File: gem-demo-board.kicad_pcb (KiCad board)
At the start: 6 copper layers, 56 x 66 mm, 151 parts, among them J1 3220-10-0100-00, J10 0473460001, J2 DF13A-2P-1.25H, J3 3220-10-0100-00, J4 2x20_Header_Female, J5 0473460001, J6 556500488, J7 556500488, J8 WE_686115148922, J9 WE_686115148922_FLIPPED, U1 MCP1700T-3302E_TT, U2 NTS0104BQ, U3 NTS0104BQ, U4 NTS0104BQ, U5 93LC56CT-IMC, U6 FT4232HQ, U7 NTB0104BQ, U8 NTB0104BQ, Y1 ASFLMB-12.000MHZ-LC-T

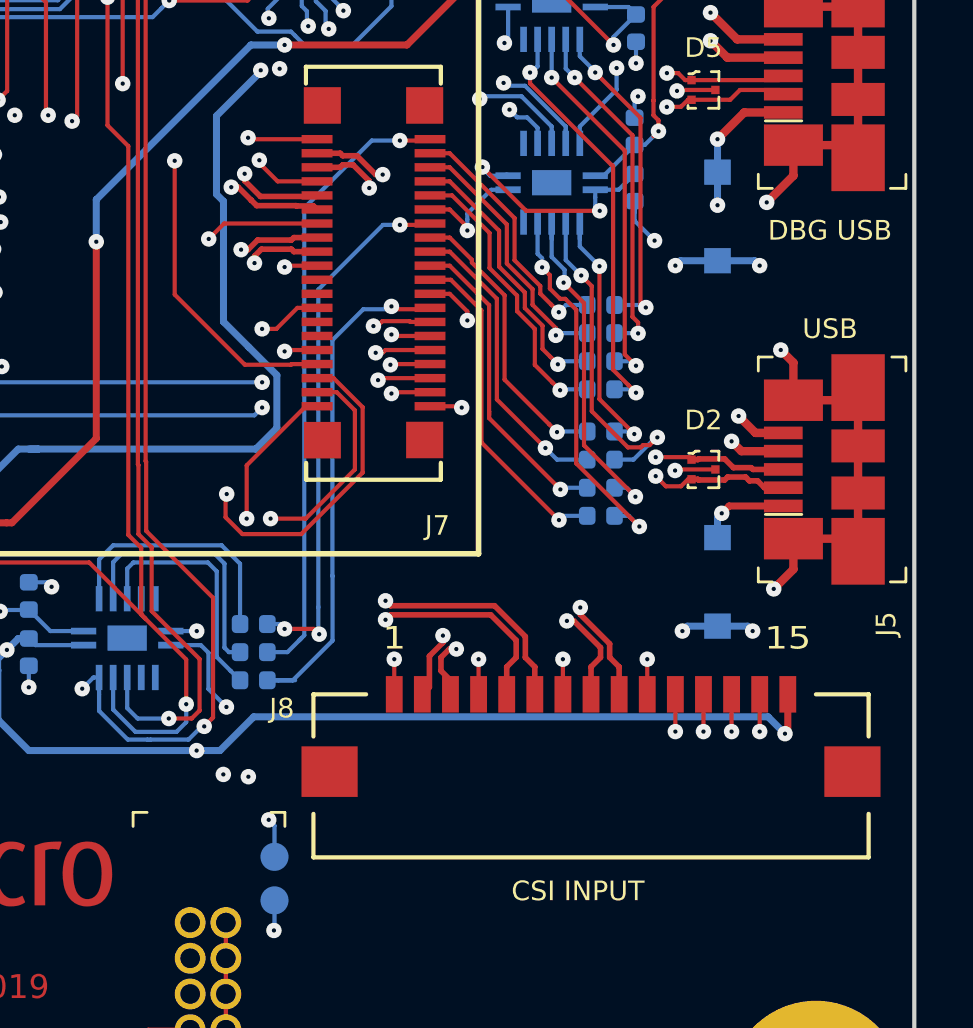
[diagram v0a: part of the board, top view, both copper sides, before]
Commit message: Flipped CSI input connector
Use camera FFC with pads on the same side now
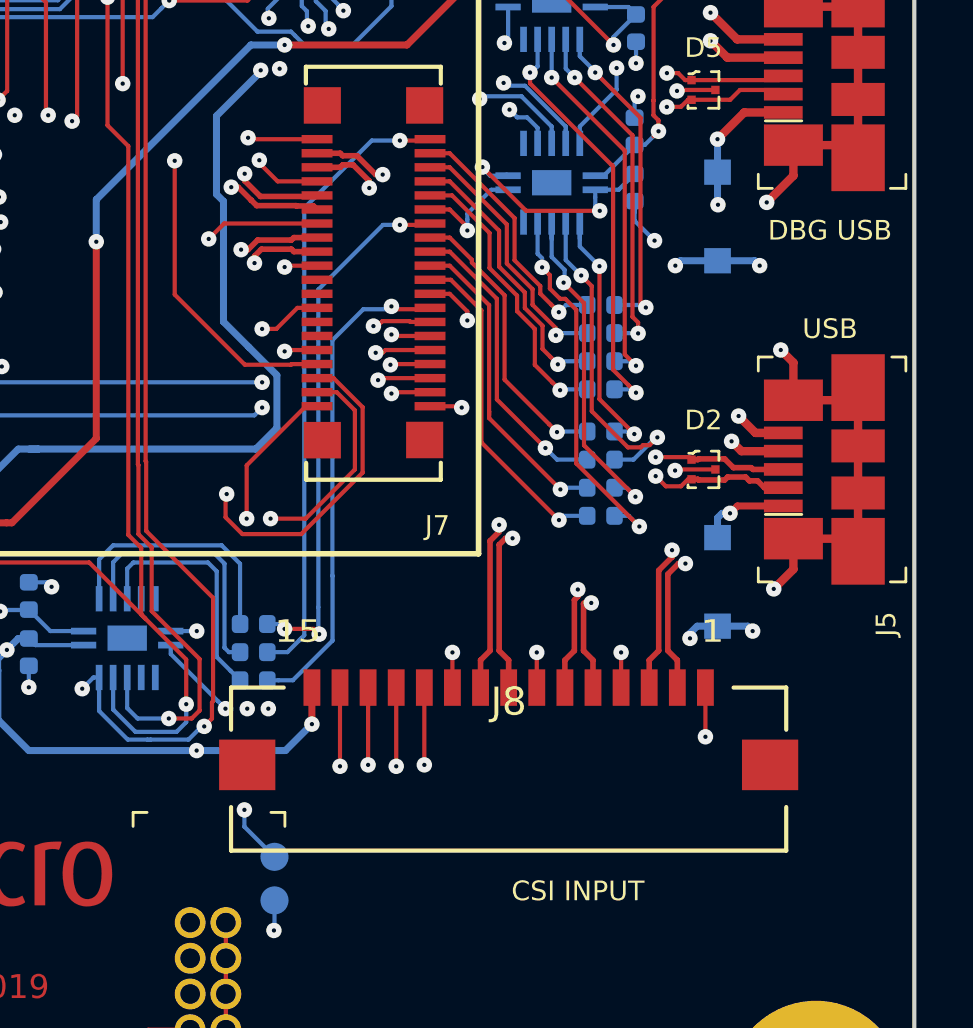
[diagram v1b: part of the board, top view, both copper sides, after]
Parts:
- J8: value WE_686115148922 -> WE_686115148922_FLIPPED; footprint zglue-demo-board-footprints:WE_686115148922 -> zglue-demo-board-footprints:WE_686115148922_FLIPPED
- moved J8 2.94 mm to (69.4, 78.0)
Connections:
- C18 pad 2: GND -> Net-(C18-Pad2)
- C19 pad 2: GND -> Net-(C19-Pad2)
- C21 pad 1: /VPHY -> Net-(C21-Pad1)
- C22 pad 1: /VPLL -> Net-(C22-Pad1)
- C25 pad 1: /VPHY -> Net-(C25-Pad1)
- C26 pad 1: /VPLL -> Net-(C26-Pad1)
- R4 pad 2: /3V3_FTDI -> Net-(R4-Pad2)
- R6 pad 2: /3V3_FTDI -> Net-(R6-Pad2)
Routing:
- net /CAM_SDA_IN: track 56.7 -> 90.8 mm
- net /3V3_SYS: track 250.6 -> 233.3 mm
- net /CAM_SCL_IN: track 56.9 -> 73.6 mm
- net /CSI_D1_IN_P: track 36.6 -> 44.7 mm
- net /CSI_D1_IN_N: track 36.6 -> 44.7 mm
- net /CAM_CLK_IN: track 20.7 -> 14.1 mm
- net /CAM_GPIO_IN: track 18.5 -> 12.7 mm
- net /CSI_D2_IN_N: track 36.6 -> 40.3 mm
- net /VCCIO3: track 84.3 -> 80.9 mm
- net /CSI_D2_IN_P: track 36.6 -> 39.8 mm
- net /CSI_CLK_IN_P: track 37.0 -> 35.3 mm
- net /CSI_CLK_IN_N: track 36.6 -> 35.3 mm
- net /DONE: track 54.9 -> 53.9 mm
- net /VCCIO2: track 66.1 -> 65.3 mm
- net GND: track 180.6 -> 179.8 mm, vias 79 -> 77
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
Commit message: Minor changes
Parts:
- moved R54 3.60 mm to (66.8, 39.5)
- moved R56 1.20 mm to (66.8, 42.0)
- moved R57 1.20 mm to (66.8, 40.8)
- moved R55 1.20 mm to (66.8, 43.1)
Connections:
- D10 pad 1: /3V3_SYS -> Net-(D10-Pad1)
- D11 pad 1: /3V3_SYS -> Net-(D11-Pad1)
- D8 pad 1: /3V3_SYS -> Net-(D8-Pad1)
- D9 pad 1: /3V3_SYS -> Net-(D9-Pad1)
- J8 pad 11: /CAM_GPIO_IN -> /3V3_SYS
- R48 pad 1: /DBG_TX -> /DBG_RX
- R49 pad 1: /DBG_RX -> /DBG_TX
- TP20 pad 1: /CAM_GPIO_IN -> /3V3_SYS
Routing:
- net /3V3_SYS: track 233.3 -> 254.3 mm, vias 19 -> 21
- net /CAM_GPIO_IN: track 12.7 -> 0.00 mm, vias 2 -> 0
- net /CSI_CLK_IN_N: track 35.3 -> 42.3 mm
- net /CSI_CLK_IN_P: track 35.3 -> 42.3 mm
- net /CAM_SDA_OUT: track 20.7 -> 17.6 mm, vias 3 -> 2
- net /CSI_D1_IN_P: track 44.7 -> 42.3 mm
- net /CSI_D1_IN_N: track 44.7 -> 42.3 mm
- net /CSI_D2_IN_P: track 39.8 -> 41.8 mm
- net /CSI_D2_IN_N: track 40.3 -> 41.8 mm
- net /I2C_1_SCL_3V3: track 20.4 -> 19.4 mm
- net /CAM_SCL_OUT: track 17.5 -> 18.5 mm
- net /DBG_TX: track 4.89 -> 5.64 mm
- net /I2C_1_SDA_3V3: track 21.6 -> 22.1 mm
- net /CAM_SDA_IN: track 90.8 -> 90.3 mm
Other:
- net class Default: clearance 0.125 -> 0.12
- rule trace_clearance: 0.125 -> 0.12

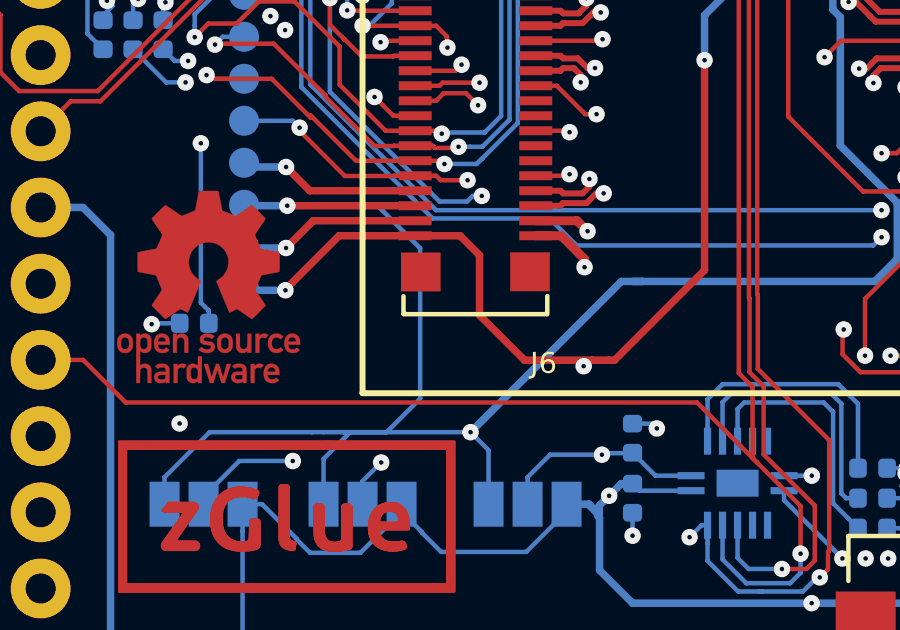
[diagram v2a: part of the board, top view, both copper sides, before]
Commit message: Disconnected 3v3_sys from GEM system chip with R60
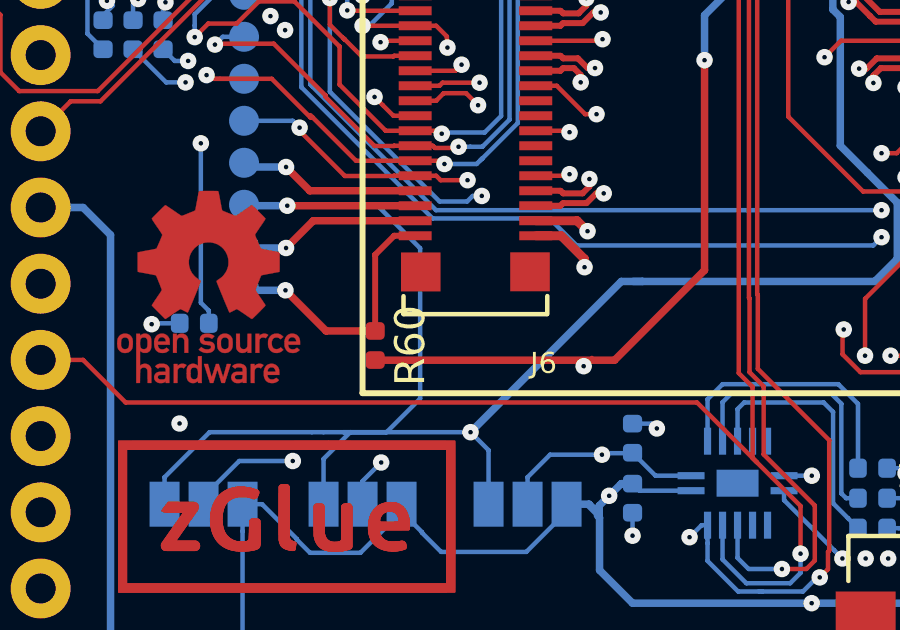
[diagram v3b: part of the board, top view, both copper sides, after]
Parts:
- added R60: R_0R_0402, zglue-demo-board-footprints:0402-res, F.Cu at (43.7, 71.7)
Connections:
- J6 pad 40: /3V3_SYS -> Net-(J6-Pad40)
- TP4 pad 1: /3V3_SYS -> Net-(J6-Pad40)
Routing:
- net Net-(J6-Pad40): track 0.00 -> 9.09 mm, vias 0 -> 1
- net /3V3_SYS: track 254.3 -> 246.2 mm, vias 21 -> 20
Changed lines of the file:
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@@
     (thickness 1.6)
     (drawings 30)
-    (tracks 4089)
+    (tracks 4087)
     (zones 0)
-    (modules 151)
-    (nets 225)
+    (modules 152)
+    (nets 226)
   )
   (page A4)
@@
   (net 223 "Net-(D10-Pad1)")
   (net 224 "Net-(D11-Pad1)")
+  (net 225 "Net-(J6-Pad40)")
   (net_class Default "This is the default net class."
     (clearance 0.12)
@@
     (add_net "Net-(J4-Pad7)")
     (add_net "Net-(J4-Pad8)")
+    (add_net "Net-(J6-Pad40)")
     (add_net "Net-(R10-Pad2)")
     (add_net "Net-(R11-Pad1)")
@@
     (add_net "Net-(U8-Pad9)")
   )
+  (module zglue-demo-board-footprints:0402-res (layer F.Cu)
+    (at 43.72 71.66 270)
+    (descr "Resistor SMD 0402 (1005 Metric), square (rectangular) end terminal, IPC_7351 nominal, (Body size source: http://www.tortai-tech.com/upload/download/2011102023233369053.pdf), generated with kicad-footprint-generator")
+    (tags resistor)
+    (attr smd)
+    (fp_text reference R60 (at 0 -1.17 90) (layer F.SilkS)
+      (effects (font (size 1 1) (thickness 0.15)))
+    )
+    (fp_text value R_0R_0402 (at 0 1.17 90) (layer F.Fab)
+      (effects (font (size 1 1) (thickness 0.15)))
+    )
+    (fp_text user %R (at 0 0 90) (layer F.Fab)
+      (effects (font (size 0.25 0.25) (thickness 0.04)))
+    )
+    (fp_line (start 0.93 0.47) (end -0.93 0.47) (layer F.CrtYd) (width 0.05))
+    (fp_line (start 0.93 -0.47) (end 0.93 0.47) (layer F.CrtYd) (width 0.05))
+    (fp_line (start -0.93 -0.47) (end 0.93 -0.47) (layer F.CrtYd) (width 0.05))
+    (fp_line (start -0.93 0.47) (end -0.93 -0.47) (layer F.CrtYd) (width 0.05))
+    (fp_line (start 0.5 0.25) (end -0.5 0.25) (layer F.Fab) (width 0.1))
+    (fp_line (start 0.5 -0.25) (end 0.5 0.25) (layer F.Fab) (width 0.1))
+    (fp_line (start -0.5 -0.25) (end 0.5 -0.25) (layer F.Fab) (width 0.1))
+    (fp_line (start -0.5 0.25) (end -0.5 -0.25) (layer F.Fab) (width 0.1))
+    (pad 2 smd roundrect (at 0.485 0 270) (size 0.59 0.64) (layers F.Cu F.Paste F.Mask) (roundrect_rratio 0.25)
+      (net 8 /3V3_SYS))
+    (pad 1 smd roundrect (at -0.485 0 270) (size 0.59 0.64) (layers F.Cu F.Paste F.Mask) (roundrect_rratio 0.25)
+      (net 225 "Net-(J6-Pad40)"))
+    (model ${KIPRJMOD}/lib/3d-models/0402-res.step
+      (offset (xyz 0 0 -0.01))
+      (scale (xyz 1 1 1))
+      (rotate (xyz 0 0 0))
+    )
+  )
   (module zglue-demo-board-footprints:WE_686115148922_FLIPPED (layer F.Cu)
     (at 69.37 78.01)
@@
     )
     (pad 1 smd circle (at 0 0.0508) (size 1 1) (layers B.Cu B.Mask)
-      (net 8 /3V3_SYS))
+      (net 225 "Net-(J6-Pad40)"))
   )
   (module zglue-demo-board-footprints:Testpoint_smd_1mm (layer B.Cu)
@@
     (fp_line (start 2.407 -7.32502) (end 2.407 -6.72502) (layer F.SilkS) (width 0.15))
     (pad 40 smd rect (at -1.99622 4.752 90) (size 0.3 1.1) (layers F.Cu F.Paste F.Mask)
-      (net 8 /3V3_SYS))
+      (net 225 "Net-(J6-Pad40)"))
     (pad 39 smd rect (at -1.99622 4.252 90) (size 0.3 1.1) (layers F.Cu F.Paste F.Mask)
       (net 34 /2V5_SYS))
@@
   (segment (start 37.058471 46.666283) (end 41.626283 46.666283) (width 0.15) (layer B.Cu) (net 8))
   (segment (start 41.626283 46.666283) (end 41.81 46.85) (width 0.15) (layer B.Cu) (net 8))
-  (segment (start 51.51 72.15) (end 51.7 72.15) (width 0.25) (layer F.Cu) (net 8))
-  (segment (start 48.7 72.15) (end 51.51 72.15) (width 0.25) (layer F.Cu) (net 8))
   (segment (start 36.45 37.65) (end 36.45 37.1) (width 0.15) (layer F.Cu) (net 8))
   (segment (start 36.45 37.1) (end 36.45 34.65) (width 0.15) (layer F.Cu) (net 8))
@@
   (segment (start 60.42 51.302844) (end 60.278032 51.160876) (width 0.15) (layer In2.Cu) (net 8))
   (segment (start 60.278032 51.160876) (end 59.889124 51.160876) (width 0.15) (layer In2.Cu) (net 8))
-  (segment (start 40.73 69.82) (end 39.4 69.82) (width 0.25) (layer B.Cu) (net 8))
-  (segment (start 39.4 69.82) (end 39.35 69.77) (width 0.25) (layer B.Cu) (net 8))
-  (segment (start 40.73 69.79) (end 40.73 69.82) (width 0.25) (layer F.Cu) (net 8))
-  (segment (start 42.518 68.002) (end 40.73 69.79) (width 0.25) (layer F.Cu) (net 8))
-  (via (at 40.73 69.82) (size 0.55) (drill 0.15) (layers F.Cu B.Cu) (net 8))
-  (segment (start 45.05378 68.002) (end 42.518 68.002) (width 0.25) (layer F.Cu) (net 8))
+  (segment (start 40.73 69.82) (end 39.4 69.82) (width 0.25) (layer B.Cu) (net 225))
+  (segment (start 39.4 69.82) (end 39.35 69.77) (width 0.25) (layer B.Cu) (net 225))
+  (via (at 40.73 69.82) (size 0.55) (drill 0.15) (layers F.Cu B.Cu) (net 225))
   (segment (start 58.27 83.32) (end 60.475001 85.525001) (width 0.15) (layer In2.Cu) (net 8))
   (segment (start 60.475001 85.525001) (end 60.475001 91.635001) (width 0.15) (layer In2.Cu) (net 8))
@@
   (segment (start 79.2 48.15) (end 79.3 48.25) (width 0.25) (layer F.Cu) (net 8))
   (via (at 79.2 45.65) (size 0.55) (drill 0.15) (layers F.Cu B.Cu) (net 8))
-  (segment (start 54.7 69.15) (end 54.7 62.15) (width 0.25) (layer F.Cu) (net 8))
   (via (at 54.7 62.15) (size 0.55) (drill 0.15) (layers F.Cu B.Cu) (net 8))
-  (segment (start 51.7 72.15) (end 54.7 69.15) (width 0.25) (layer F.Cu) (net 8))
-  (segment (start 47.2 70.65) (end 48.7 72.15) (width 0.25) (layer F.Cu) (net 8))
-  (segment (start 47.2 68.65) (end 47.2 70.65) (width 0.25) (layer F.Cu) (net 8))
-  (segment (start 46.552 68.002) (end 47.2 68.65) (width 0.25) (layer F.Cu) (net 8))
-  (segment (start 45.05378 68.002) (end 46.552 68.002) (width 0.25) (layer F.Cu) (net 8))
   (segment (start 73.85 58.705) (end 72.755 59.8) (width 0.15) (layer B.Cu) (net 8))
   (segment (start 72.755 59.8) (end 72.45 59.8) (width 0.15) (layer B.Cu) (net 8))
@@
   (segment (start 62.19 85.1808) (end 62.19 91.91) (width 0.15) (layer B.Cu) (net 8))
   (segment (start 61.04 84.0308) (end 62.19 85.1808) (width 0.15) (layer B.Cu) (net 8))
+  (segment (start 54.7 69.15) (end 54.7 62.15) (width 0.25) (layer F.Cu) (net 8))
+  (segment (start 51.7 72.15) (end 54.7 69.15) (width 0.25) (layer F.Cu) (net 8))
+  (segment (start 43.72 72.145) (end 43.725 72.15) (width 0.25) (layer F.Cu) (net 8))
+  (segment (start 43.725 72.15) (end 51.7 72.15) (width 0.25) (layer F.Cu) (net 8))
   (segment (start 44.636987 31.499989) (end 39.458087 31.499989) (width 0.15) (layer In2.Cu) (net 84))
   (segment (start 47.881999 32.654999) (end 47.086998 33.45) (width 0.15) (layer In2.Cu) (net 84))
@@
   (via (at 54.36 46.95) (size 0.55) (drill 0.15) (layers F.Cu B.Cu) (net 214))
   (segment (start 53.785 46.85) (end 54.26 46.85) (width 0.15) (layer B.Cu) (net 214))
+  (segment (start 44.35378 68.002) (end 45.05378 68.002) (width 0.2) (layer F.Cu) (net 225))
+  (segment (start 43.72 71.175) (end 43.72 68.63578) (width 0.2) (layer F.Cu) (net 225))
+  (segment (start 43.72 68.63578) (end 44.35378 68.002) (width 0.2) (layer F.Cu) (net 225))
+  (segment (start 42.085 71.175) (end 40.73 69.82) (width 0.25) (layer F.Cu) (net 225))
+  (segment (start 43.72 71.175) (end 42.085 71.175) (width 0.25) (layer F.Cu) (net 225))
   (zone (net 2) (net_name GND) (layer In4.Cu) (hatch edge 0.508)
     (connect_pads (clearance 0.15))

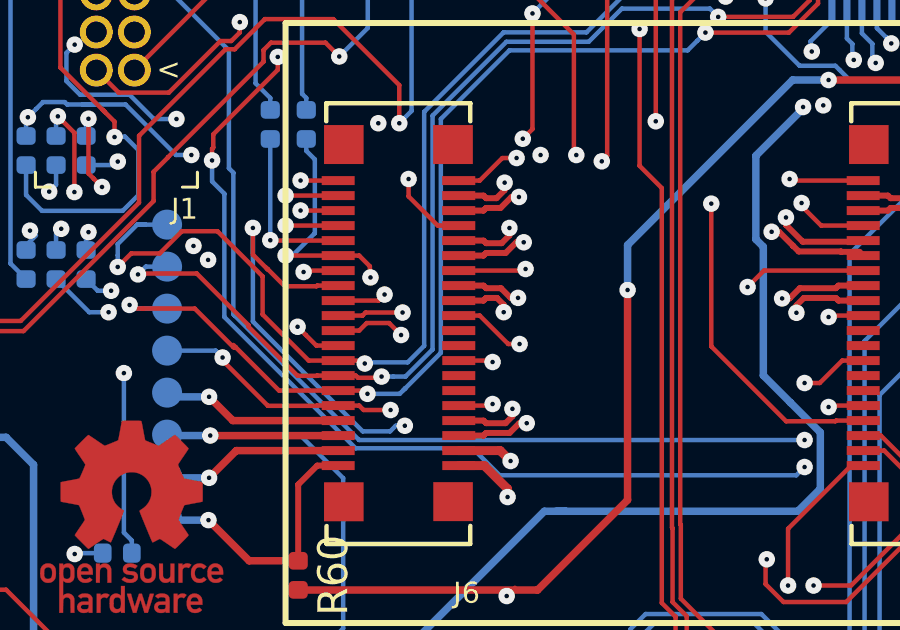
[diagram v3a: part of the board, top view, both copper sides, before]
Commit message: Connect CSI_D1_IN_P to I2C_1_SDA through R61
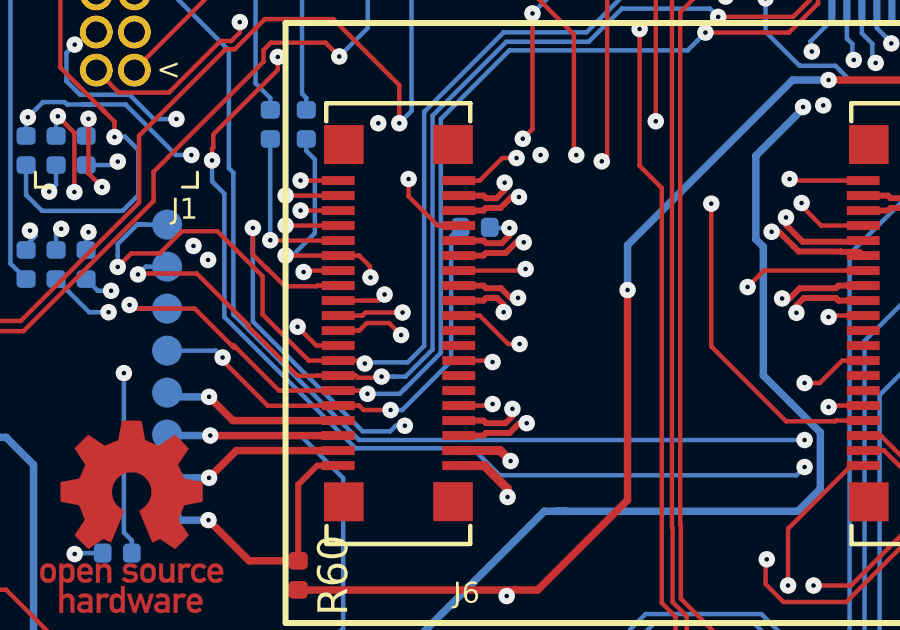
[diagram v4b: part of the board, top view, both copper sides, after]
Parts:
- added R61: R_220R_0402, antmicro-footprints:0402-res, B.Cu at (49.6, 60.1)
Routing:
- net /I2C_1_SDA: track 83.6 -> 90.9 mm
- net /CSI_D1_IN_P: track 42.3 -> 43.0 mm

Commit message: Exported R_220R to local library
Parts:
- R61: footprint antmicro-footprints:0402-res -> gem-demo-board-footprints:0402-res
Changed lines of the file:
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@@
     (add_net "Net-(U8-Pad9)")
   )
-  (module antmicro-footprints:0402-res (layer B.Cu)
+  (module gem-demo-board-footprints:0402-res (layer B.Cu)
     (at 49.62 60.06 180)
     (descr "Resistor SMD 0402 (1005 Metric), square (rectangular) end terminal, IPC_7351 nominal, (Body size source: http://www.tortai-tech.com/upload/download/2011102023233369053.pdf), generated with kicad-footprint-generator")

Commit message: Updated rev. number and date
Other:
- board text added: "Rev. 1.2 01/2020"
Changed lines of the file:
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@@
     (effects (font (size 0.85 0.85) (thickness 0.18)))
   )
-  (gr_text "Rev. 1.1  11/2019" (at 47.835 88.66) (layer F.Cu)
+  (gr_text "Rev. 1.2  01/2020" (at 47.835 88.66) (layer F.Cu)
     (effects (font (size 0.85 0.85) (thickness 0.18)))
   )
